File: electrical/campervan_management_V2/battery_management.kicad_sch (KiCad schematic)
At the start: 17 parts, among them K1 G6KU-2, Q3 MDD2302, Q4 MMBT2222A, Q5 MDD2302, Q6 MMBT2222A, U13 LTV-817S-TA1-C

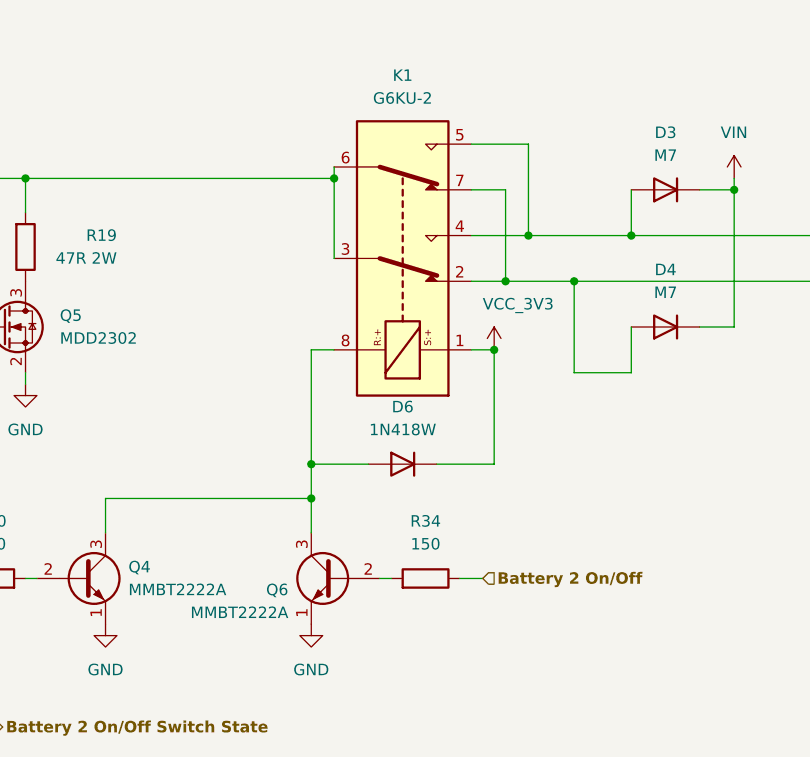
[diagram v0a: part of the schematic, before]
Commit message: Changed to high side relay drive and added 4.1V PS for high side relay hold
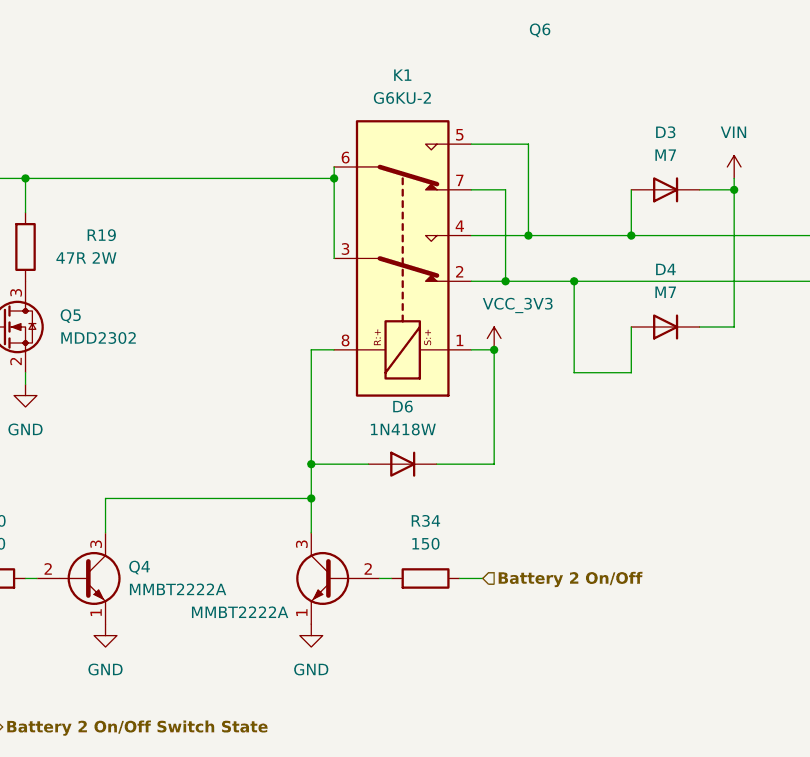
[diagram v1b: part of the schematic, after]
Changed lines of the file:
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@@
 		(dnp no)
 		(property "Reference" "Q6"
-			(at 127 93.98 0)
+			(at 156.21 31.75 0)
 			(effects
 				(font

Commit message: updated
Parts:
- removed C28: 100nF, Capacitor_SMD:C_0805_2012Metric, symbol Device:C_Small
- removed Q3, Q5: MDD2302, Package_TO_SOT_SMD:SOT-23, symbol camper_van:MDD2302
- removed R19: 47R 2W, Resistor_SMD:R_2512_6332Metric, symbol Device:R
- removed R40, R43: 4k7, Resistor_SMD:R_0805_2012Metric, symbol Device:R
- added C20: 100nF, Capacitor_SMD:C_0805_2012Metric, symbol Device:C_Small
- added D5, D7: M7, Diode_SMD:D_SMA, symbol Diode:1N4001
- added Q1, Q2: Q_PMOS_DGS, Package_TO_SOT_SMD:SOT-23, symbol Transistor_FET:Q_PMOS_DGS
- added R20: 47k, Resistor_SMD:R_0805_2012Metric, symbol Device:R
- added R22: 150, Resistor_SMD:R_0805_2012Metric, symbol Device:R
- added R6: 1M, Resistor_SMD:R_0805_2012Metric, symbol Device:R
- added U3: LTV-817S-TA1-C, Package_SO:SO-4_4.4x3.6mm_P2.54mm, symbol Isolator:LTV-357T
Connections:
- net Batteries On: now also R22.1
- net GND: now also D3.2 (A), D4.2 (A), D7.2 (A), U3.2, U3.3
- net at K1.3, K1.6: now also D5.1 (K), D7.1 (K), Q2.1 (D)
- net Battery 1 renamed Battery 1 Relay
- net Battery 1 Relay: now also D3.1 (K); no longer D3.2 (A)
- net Battery 2 renamed Battery 2 Relay
- net Battery 2 Relay: now also D4.1 (K); no longer D4.2 (A)
- removed net VIN: D3.1 (K), D4.1 (K)
- new net: C20.1, Q2.2 (G), R6.2
- new net: C20.2, Q1.2 (G), R20.2, U3.4
- new net: R22.2, U3.1
- new net: D5.2 (A), Q1.1 (D)
- new net Power On Switch - 4V1: Q2.3 (S), R20.1, R6.1
- new net Power On Switch - Vin: Q1.3 (S)
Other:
- moved on the sheet: C30, D3, D4, D6, K1, Q4, Q6, R29, R30, R34, U13

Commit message: First attempt at PCB layout
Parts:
- renumbered C20 to C22, C30 to C32, D7 to D1, D5 to D2, D4 to D5, D3 to D7, Q2 to Q3, Q1 to Q4, Q4 to Q7, Q6 to Q8, R29 to R11, R6 to R12, R20 to R15, R30 to R45, R34 to R51, R22 to R56, U3 to U25, U13 to U6
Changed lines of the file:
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@@
 		(on_board yes)
 		(dnp no)
-		(property "Reference" "C20"
+		(property "Reference" "C22"
 			(at 86.3538 62.23 0)
 			(effects
@@
 			(project "campervan_management_V2"
 				(path "/870a08cc-a6e6-4310-b4b3-ae6af01530aa/2161f18b-f003-4e01-bf58-6b158195d61c"
-					(reference "C20")
+					(reference "C22")
 					(unit 1)
 				)
@@
 		(on_board yes)
 		(dnp no)
-		(property "Reference" "U13"
+		(property "Reference" "U6"
 			(at 64.77 99.06 0)
 			(effects
@@
 			(project "campervan_management_V2"
 				(path "/870a08cc-a6e6-4310-b4b3-ae6af01530aa/2161f18b-f003-4e01-bf58-6b158195d61c"
-					(reference "U13")
+					(reference "U6")
 					(unit 1)
 				)
@@
 		(dnp no)
 		(fields_autoplaced yes)
-		(property "Reference" "R22"
+		(property "Reference" "R56"
 			(at 58.42 53.34 90)
 			(effects
@@
 			(project "campervan_management_V2"
 				(path "/870a08cc-a6e6-4310-b4b3-ae6af01530aa/2161f18b-f003-4e01-bf58-6b158195d61c"
-					(reference "R22")
+					(reference "R56")
 					(unit 1)
 				)
@@
 		(on_board yes)
 		(dnp no)
-		(property "Reference" "R20"
+		(property "Reference" "R15"
 			(at 82.55 45.7199 0)
 			(effects
@@
 			(project "campervan_management_V2"
 				(path "/870a08cc-a6e6-4310-b4b3-ae6af01530aa/2161f18b-f003-4e01-bf58-6b158195d61c"
-					(reference "R20")
+					(reference "R15")
 					(unit 1)
 				)
@@
 		(dnp no)
 		(fields_autoplaced yes)
-		(property "Reference" "Q4"
+		(property "Reference" "Q7"
 			(at 111.76 109.2199 0)
 			(effects
@@
 			(project "campervan_management_V2"
 				(path "/870a08cc-a6e6-4310-b4b3-ae6af01530aa/2161f18b-f003-4e01-bf58-6b158195d61c"
-					(reference "Q4")
+					(reference "Q7")
 					(unit 1)
 				)
@@
 		(on_board yes)
 		(dnp no)
-		(property "Reference" "C30"
+		(property "Reference" "C32"
 			(at 72.39 114.3062 0)
 			(effects
@@
 			(project "campervan_management_V2"
 				(path "/870a08cc-a6e6-4310-b4b3-ae6af01530aa/2161f18b-f003-4e01-bf58-6b158195d61c"
-					(reference "C30")
+					(reference "C32")
 					(unit 1)
 				)
@@
 		(dnp no)
 		(fields_autoplaced yes)
-		(property "Reference" "R6"
+		(property "Reference" "R12"
 			(at 92.71 45.7199 0)
 			(effects
@@
 			(project "campervan_management_V2"
 				(path "/870a08cc-a6e6-4310-b4b3-ae6af01530aa/2161f18b-f003-4e01-bf58-6b158195d61c"
-					(reference "R6")
+					(reference "R12")
 					(unit 1)
 				)
@@
 		(on_board yes)
 		(dnp no)
-		(property "Reference" "Q1"
+		(property "Reference" "Q4"
 			(at 121.92 60.9601 0)
 			(effects
@@
 			(project "campervan_management_V2"
 				(path "/870a08cc-a6e6-4310-b4b3-ae6af01530aa/2161f18b-f003-4e01-bf58-6b158195d61c"
-					(reference "Q1")
+					(reference "Q4")
 					(unit 1)
 				)
@@
 		(on_board yes)
 		(dnp no)
-		(property "Reference" "Q2"
+		(property "Reference" "Q3"
 			(at 102.87 60.9601 0)
 			(effects
@@
 			(project "campervan_management_V2"
 				(path "/870a08cc-a6e6-4310-b4b3-ae6af01530aa/2161f18b-f003-4e01-bf58-6b158195d61c"
-					(reference "Q2")
+					(reference "Q3")
 					(unit 1)
 				)
@@
 		(on_board yes)
 		(dnp no)
-		(property "Reference" "U3"
+		(property "Reference" "U25"
 			(at 69.85 53.34 0)
 			(effects
@@
 			(project "campervan_management_V2"
 				(path "/870a08cc-a6e6-4310-b4b3-ae6af01530aa/2161f18b-f003-4e01-bf58-6b158195d61c"
-					(reference "U3")
+					(reference "U25")
 					(unit 1)
 				)
@@
 		(dnp no)
 		(fields_autoplaced yes)
-		(property "Reference" "D4"
+		(property "Reference" "D5"
 			(at 172.72 88.8999 90)
 			(effects
@@
 			(project "campervan_management_V2"
 				(path "/870a08cc-a6e6-4310-b4b3-ae6af01530aa/2161f18b-f003-4e01-bf58-6b158195d61c"
-					(reference "D4")
+					(reference "D5")
 					(unit 1)
 				)
@@
 		(dnp no)
 		(fields_autoplaced yes)
-		(property "Reference" "D5"
+		(property "Reference" "D2"
 			(at 115.57 67.3099 90)
 			(effects
@@
 			(project "campervan_management_V2"
 				(path "/870a08cc-a6e6-4310-b4b3-ae6af01530aa/2161f18b-f003-4e01-bf58-6b158195d61c"
-					(reference "D5")
+					(reference "D2")
 					(unit 1)
 				)
@@
 		(dnp no)
 		(fields_autoplaced yes)
-		(property "Reference" "R34"
+		(property "Reference" "R51"
 			(at 144.78 104.14 90)
 			(effects
@@
 			(project "campervan_management_V2"
 				(path "/870a08cc-a6e6-4310-b4b3-ae6af01530aa/2161f18b-f003-4e01-bf58-6b158195d61c"
-					(reference "R34")
+					(reference "R51")
 					(unit 1)
 				)
@@
 		(dnp no)
 		(fields_autoplaced yes)
-		(property "Reference" "D7"
+		(property "Reference" "D1"
 			(at 111.76 77.4699 90)
 			(effects
@@
 			(project "campervan_management_V2"
 				(path "/870a08cc-a6e6-4310-b4b3-ae6af01530aa/2161f18b-f003-4e01-bf58-6b158195d61c"
-					(reference "D7")
+					(reference "D1")
 					(unit 1)
 				)
@@
 		(on_board yes)
 		(dnp no)
-		(property "Reference" "R30"
+		(property "Reference" "R45"
 			(at 96.52 104.14 90)
 			(effects
@@
 			(project "campervan_management_V2"
 				(path "/870a08cc-a6e6-4310-b4b3-ae6af01530aa/2161f18b-f003-4e01-bf58-6b158195d61c"
-					(reference "R30")
+					(reference "R45")
 					(unit 1)
 				)
@@
 		(dnp no)
 		(fields_autoplaced yes)
-		(property "Reference" "R29"
+		(property "Reference" "R11"
 			(at 50.8 99.06 90)
 			(effects
@@
 			(project "campervan_management_V2"
 				(path "/870a08cc-a6e6-4310-b4b3-ae6af01530aa/2161f18b-f003-4e01-bf58-6b158195d61c"
-					(reference "R29")
+					(reference "R11")
 					(unit 1)
 				)
@@
 		(on_board yes)
 		(dnp no)
-		(property "Reference" "Q6"
+		(property "Reference" "Q8"
 			(at 158.75 49.53 0)
 			(effects
@@
 			(project "campervan_management_V2"
 				(path "/870a08cc-a6e6-4310-b4b3-ae6af01530aa/2161f18b-f003-4e01-bf58-6b158195d61c"
-					(reference "Q6")
+					(reference "Q8")
 					(unit 1)
 				)
@@
 		(dnp no)
 		(fields_autoplaced yes)
-		(property "Reference" "D3"
+		(property "Reference" "D7"
 			(at 181.61 88.8999 90)
 			(effects
@@
 			(project "campervan_management_V2"
 				(path "/870a08cc-a6e6-4310-b4b3-ae6af01530aa/2161f18b-f003-4e01-bf58-6b158195d61c"
-					(reference "D3")
-					(unit 1)
-				)
+					(reference "D7")
+					(unit 1)
+				)

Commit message: Close to final design
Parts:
- removed K1: G6KU-2, Relay_SMD:Relay_DPDT_Omron_G6K-2F-Y, symbol Relay:G6KU-2
- removed Q3, Q4: Q_PMOS_DGS, Package_TO_SOT_SMD:SOT-23, symbol Transistor_FET:Q_PMOS_DGS
- added K1: G5V-2, Relay_THT:Relay_DPDT_Omron_G5V-2, symbol Relay:G5V-2
- added Q5, Q6: FDS4685, Package_SO:SOIC-8_3.9x4.9mm_P1.27mm, symbol Transistor_FET:FDS9435A
- R24: renamed from R15; LCSC PN C17520 -> C17713
- renumbered C22 to C19, C32 to C20, D7 to D10, D1 to D6, D2 to D7, D5 to D8, D6 to D9, R11 to R14, R12 to R22, R56 to R26, R45 to R29, R51 to R30, U25 to U15
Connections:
- net Battery 1 Relay: now also K1.8, K1.9
- net Battery 2 Relay: now also K1.11, K1.6
- net Power On Switch - 4V1: now also Q5.1 (S), Q5.2 (S), Q5.3 (S)
- net Power On Switch - Vin: now also Q6.1 (S), Q6.2 (S), Q6.3 (S)
- net VCC_3V3: now also K1.1
- net at D9.2 (A), Q7.3 (C), Q8.3 (C): now also K1.16
- net at C19.1, R22.2: now also Q5.4 (G)
- net at C19.2, R24.2, U15.4: now also Q6.4 (G)
- net Net-(R27-Pad2): now reaches R26.2, U15.1
- net at D7.2 (A): now also Q6.5 (D), Q6.6 (D), Q6.7 (D), Q6.8 (D)
- net at D6.1 (K), D7.1 (K): now also K1.13, K1.4, Q5.5 (D), Q5.6 (D), Q5.7 (D), Q5.8 (D)
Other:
- moved on the sheet: R26, U15
